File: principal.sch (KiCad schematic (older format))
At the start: 39 parts, among them J1 TB_1X2, P2 CONN_02X01, Q1 2N7002, Q2 2N7002, Q3 2N7002, Q4 2N7002, U1 24LC64, U2 LM2596, U3 NCP1117ST33T3G, U4 Buzzer

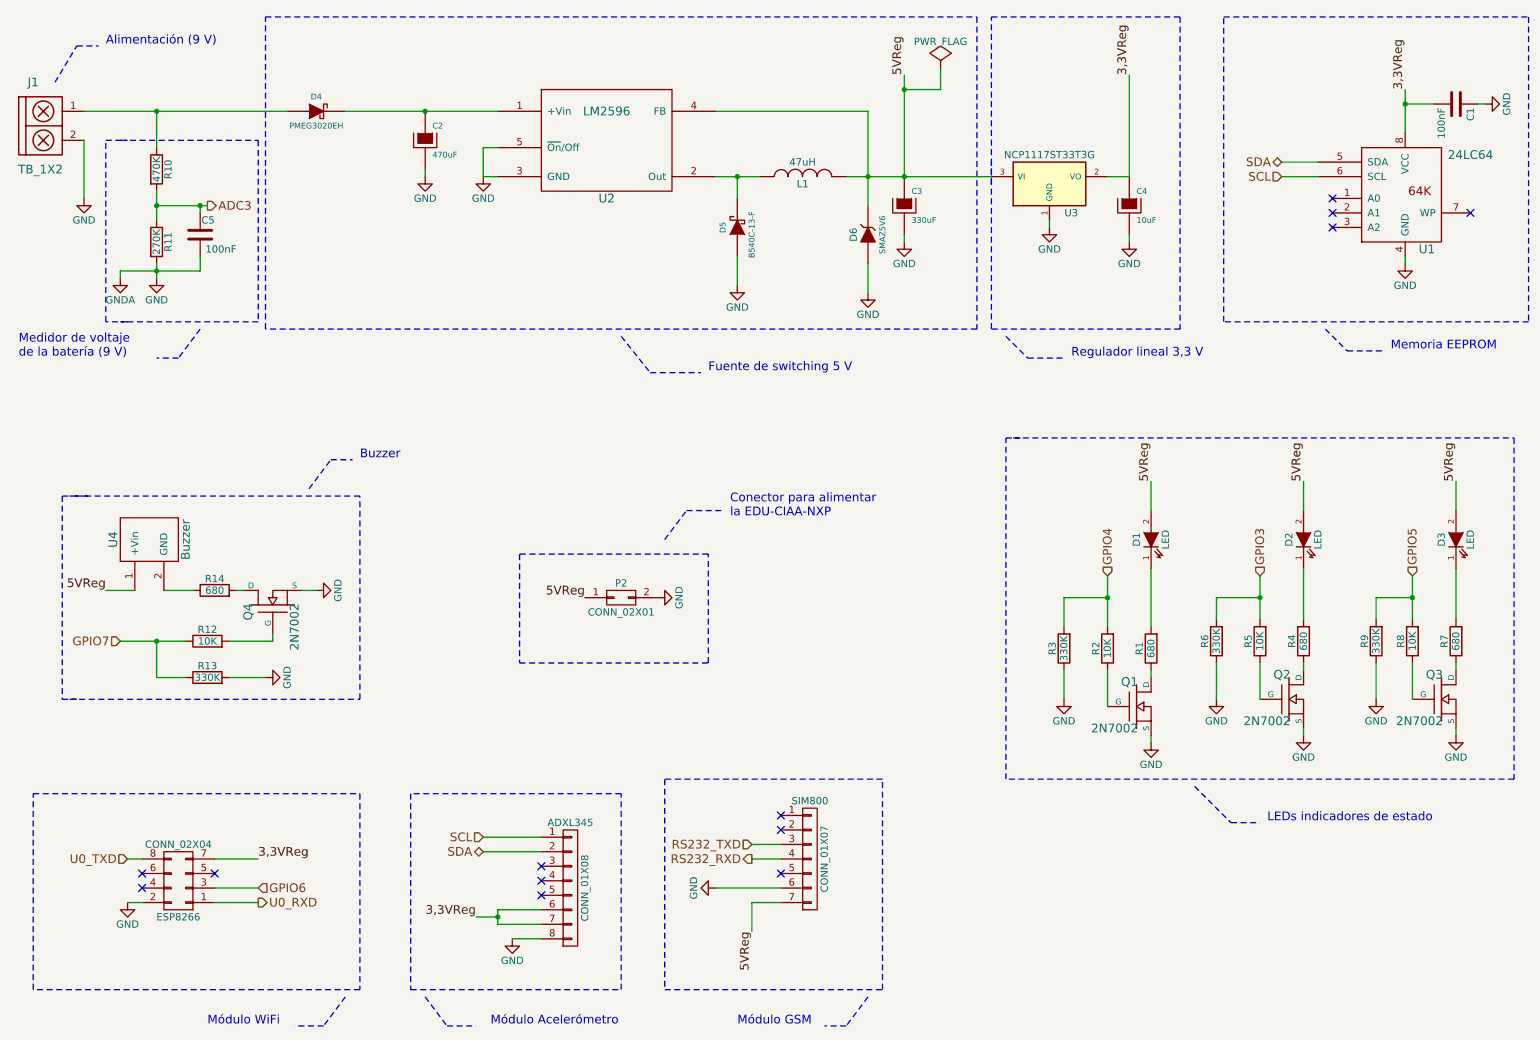
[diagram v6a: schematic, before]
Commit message: Realizando las correcciones correspondientes a la Revision 1
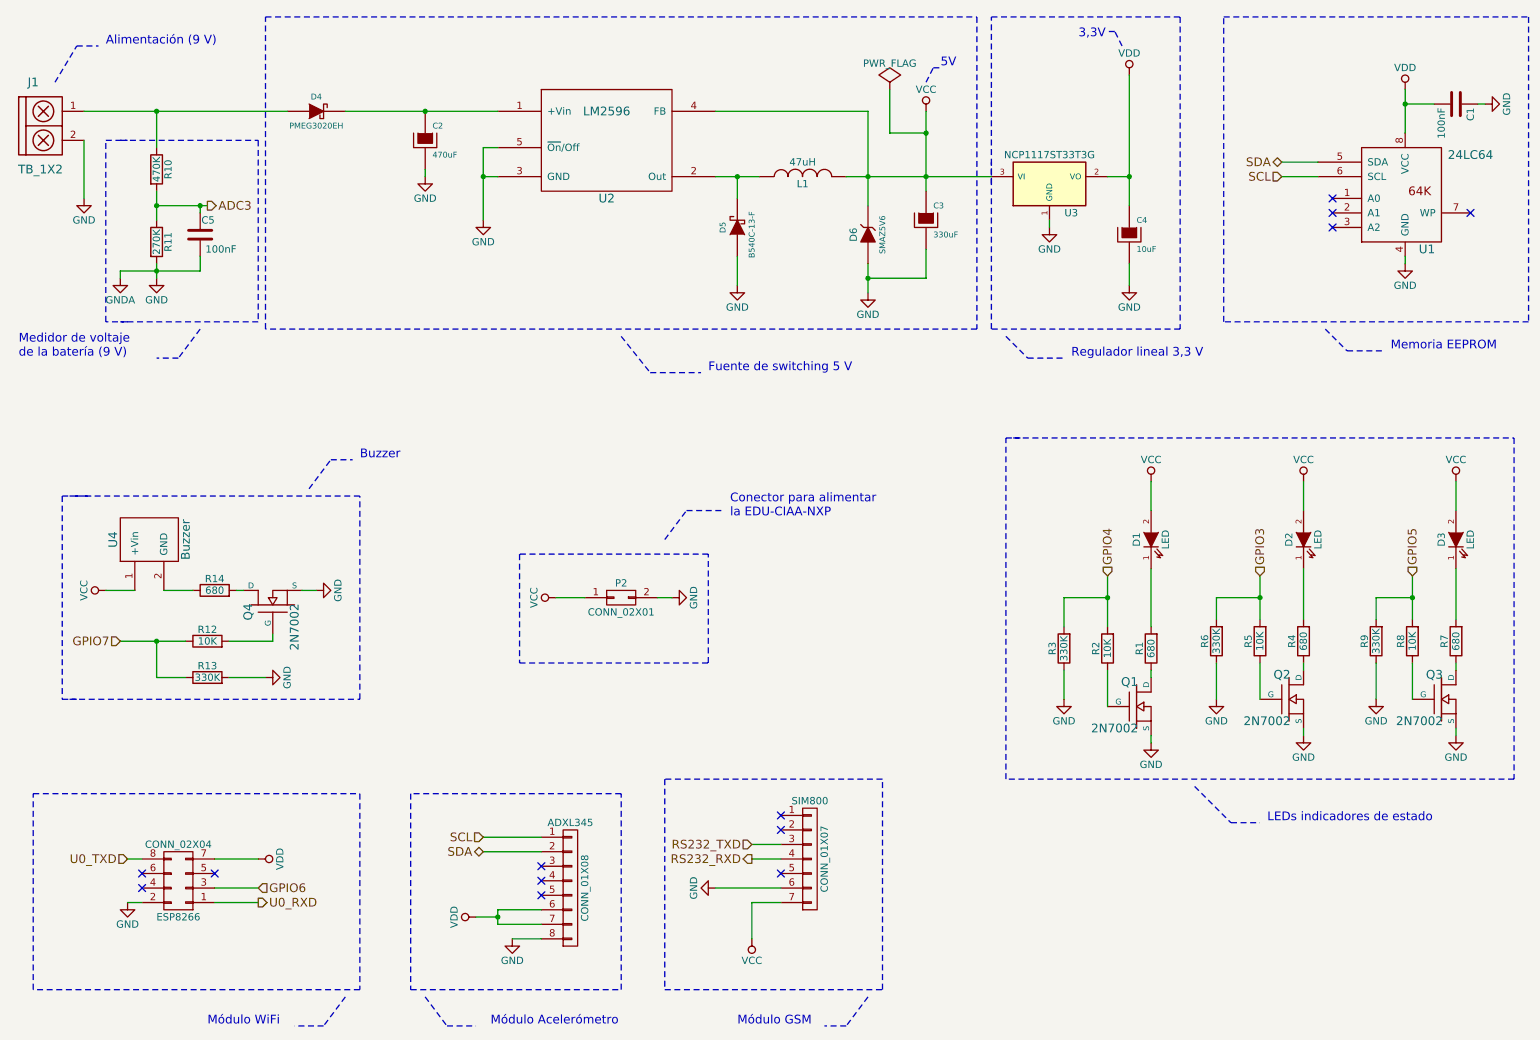
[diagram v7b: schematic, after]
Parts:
- ADXL345: footprint Pin_Headers:Pin_Header_Straight_1x08 -> footprints:adxl345
- ESP8266: footprint Pin_Headers:Pin_Header_Straight_2x04 -> footprints:esp8266
- SIM800: footprint Pin_Headers:Pin_Header_Straight_1x07 -> footprints:sim800l
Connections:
- net 3,3VReg renamed VDD
- net 5VReg renamed VCC
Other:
- note added: "3,3V"
- note added: "5V"
- moved on the sheet: C3, C4

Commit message: Revisión 1.0 terminada
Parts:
- C1, C5: footprint Capacitors_SMD:C_0805_HandSoldering -> footprints:C_0805_HandSoldering
- C2: footprint mod:c2 -> footprints:c2
- C3: footprint mod:c3 -> footprints:c3
- C4: footprint Capacitors_Tantalum_SMD:TantalC_SizeA_EIA-3216_HandSoldering -> footprints:TantalC_SizeA_EIA-3216_HandSoldering
- D1, D2, D3: footprint LEDs:LED-3MM -> footprints:LED-3MM
- D4, D6: footprint mod:SOD123F -> footprints:SOD123F
- D5: footprint mod:SMC_Handsoldering -> footprints:SMC_Handsoldering
- J1: footprint mod:bornier2 -> footprints:bornier2
- L1: footprint mod:SRN1060 -> footprints:SRN1060
- P2: footprint Pin_Headers:Pin_Header_Straight_2x01 -> footprints:Pin_Header_Straight_2x01
- Q1, Q2, Q3, Q4: footprint TO_SOT_Packages_SMD:SOT-23_Handsoldering -> footprints:SOT-23_Handsoldering
- R1, R10, R11, R12, R13, R14, R2, R3, R4, R5, R6, R7, R8, R9: footprint Resistors_SMD:R_0805_HandSoldering -> footprints:R_0805_HandSoldering
- U1: footprint Housings_SOIC:SOIC-8_3.9x4.9mm_Pitch1.27mm -> footprints:SOIC-8_3.9x4.9mm_Pitch1.27mm
- U2: footprint TO_SOT_Packages_SMD:TO-263-5Lead -> footprints:TO-263-5Lead
- U3: footprint TO_SOT_Packages_SMD:SOT-223 -> footprints:SOT-223
- U4: Digikey# (none) -> 433-1029-ND; Manf (none) -> Soberton Inc.; Manf# (none) -> WST-1205S
